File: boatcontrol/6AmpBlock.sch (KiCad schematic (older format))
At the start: 13 parts, among them U7901 ULN2803A

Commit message: Switch resistors
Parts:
- removed C7901, C7902, C7903, C7904, C7905, C7906, C7907, C7908: 107CKS016M 100UF, Capacitor_THT:CP_Radial_D5.0mm_P2.00mm, symbol Device:C_Small
- removed RN7901, RN7904: 4116R-1-103LF, DIP787W49P254L2197H469Q16N, symbol BoatControl:4116R-1-103LF
- removed RN7903: 4120R-1-103LF, BoatControl:DIP254P762X432-16P, symbol Device:R_Pack08
- added C5201, C5202, C5203, C5204, C5205, C5206, C5207, C5208: 1uF, Capacitor_THT:C_Disc_D7.5mm_W5.0mm_P5.00mm, symbol Device:C_Small
- added RN?: 10M Ohm, Resistor_THT:R_Array_SIP9, symbol Device:R_Network08
- added RN? (x2): 100K Ohm, Resistor_THT:R_Array_SIP9, symbol Device:R_Network08
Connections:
- wire segments 226 -> 205

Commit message: Resistance is futile
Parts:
- gave numbers to parts that had none: 3
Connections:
- net +5V: now also RN7904.1 (common)
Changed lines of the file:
@@
 $Descr A4 11693 8268
 encoding utf-8
-Sheet 79 87
+Sheet 52 87
 Title "Boat Control Hat"
 Date "2020-07-09"
@@
 AR Path="/D1BB8DB4/5F317CB5/60365AE4" Ref="#PWR07901"  Part="1"
 AR Path="/D1BB8DB4/5F746103/60365AE4" Ref="#PWR05201"  Part="1"
-F 0 "#PWR07901" H 6700 3400 50  0001 C CNN
+F 0 "#PWR05201" H 6700 3400 50  0001 C CNN
 F 1 "+12P" H 6550 3650 50  0000 C CNN
 F 2 "" H 6700 3550 50  0001 C CNN
@@
 AR Path="/D1BB8DB4/5F317CB5/60365AF1" Ref="U7901"  Part="1"
 AR Path="/D1BB8DB4/5F746103/60365AF1" Ref="U5201"  Part="1"
-F 0 "U7901" H 6250 3650 50  0000 L CNN
+F 0 "U5201" H 6250 3650 50  0000 L CNN
 F 1 "ULN2803A" H 6100 4350 50  0000 L CNN
 F 2 "Package_DIP:DIP-18_W7.62mm" H 6350 3200 50  0001 L CNN
@@
 AR Path="/D1BB8DB4/5F317CB5/60365B03" Ref="#PWR07902"  Part="1"
 AR Path="/D1BB8DB4/5F746103/60365B03" Ref="#PWR05202"  Part="1"
-F 0 "#PWR07902" H 6300 4300 50  0001 C CNN
+F 0 "#PWR05202" H 6300 4300 50  0001 C CNN
 F 1 "GND" H 6305 4377 50  0000 C CNN
 F 2 "" H 6300 4550 50  0001 C CNN
@@
 AR Path="/D1BB8DB4/5F317CB5/60365B8C" Ref="#PWR07903"  Part="1"
 AR Path="/D1BB8DB4/5F746103/60365B8C" Ref="#PWR05203"  Part="1"
-F 0 "#PWR07903" H 2250 5150 50  0001 C CNN
+F 0 "#PWR05203" H 2250 5150 50  0001 C CNN
 F 1 "+5V" H 2265 5473 50  0000 C CNN
 F 2 "" H 2250 5300 50  0001 C CNN
@@
 AR Path="/D1BB8DB4/5F317CB5/60365C68" Ref="RN7902"  Part="1"
 AR Path="/D1BB8DB4/5F746103/60365C68" Ref="RN5202"  Part="1"
-F 0 "RN7902" V 7000 4050 50  0000 L CNN
+F 0 "RN5202" V 7000 4050 50  0000 L CNN
 F 1 "4116R-1-471" V 7000 3900 50  0001 L CNN
 F 2 "BoatControl:DIP254P762X432-16P" V 7975 4050 50  0001 C CNN
@@
 AR Path="/D1BB8DB4/5F746103/62AB509B" Ref="C5201"  Part="1"
 AR Path="/D1BB8DB4/5F317CB5/62AB509B" Ref="C7901"  Part="1"
-F 0 "C7901" V 4400 2700 50  0000 L CNN
+F 0 "C5201" V 4400 2700 50  0000 L CNN
 F 1 "1uF" H 3600 2550 50  0001 L CNN
 F 2 "Capacitor_THT:C_Disc_D7.5mm_W5.0mm_P5.00mm" H 4450 2650 50  0001 C CNN
@@
 AR Path="/D1BB8DB4/5F746103/62AC1E93" Ref="C5202"  Part="1"
 AR Path="/D1BB8DB4/5F317CB5/62AC1E93" Ref="C7902"  Part="1"
-F 0 "C7902" V 4400 2900 50  0000 L CNN
+F 0 "C5202" V 4400 2900 50  0000 L CNN
 F 1 "1uF" H 3600 2750 50  0001 L CNN
 F 2 "Capacitor_THT:C_Disc_D7.5mm_W5.0mm_P5.00mm" H 4450 2850 50  0001 C CNN
@@
 AR Path="/D1BB8DB4/5F746103/62ADD9A6" Ref="C5208"  Part="1"
 AR Path="/D1BB8DB4/5F317CB5/62ADD9A6" Ref="C7908"  Part="1"
-F 0 "C7908" V 4400 5900 50  0000 L CNN
+F 0 "C5208" V 4400 5900 50  0000 L CNN
 F 1 "1uF" H 3600 5750 50  0001 L CNN
 F 2 "Capacitor_THT:C_Disc_D7.5mm_W5.0mm_P5.00mm" H 4450 5850 50  0001 C CNN
@@
 AR Path="/D1BB8DB4/5F746103/62AEACF8" Ref="C5207"  Part="1"
 AR Path="/D1BB8DB4/5F317CB5/62AEACF8" Ref="C7907"  Part="1"
-F 0 "C7907" V 4400 5700 50  0000 L CNN
+F 0 "C5207" V 4400 5700 50  0000 L CNN
 F 1 "1uF" H 3600 5550 50  0001 L CNN
 F 2 "Capacitor_THT:C_Disc_D7.5mm_W5.0mm_P5.00mm" H 4450 5650 50  0001 C CNN
@@
 AR Path="/D1BB8DB4/5F746103/62AF81A3" Ref="C5206"  Part="1"
 AR Path="/D1BB8DB4/5F317CB5/62AF81A3" Ref="C7906"  Part="1"
-F 0 "C7906" V 4400 4900 50  0000 L CNN
+F 0 "C5206" V 4400 4900 50  0000 L CNN
 F 1 "1uF" H 3600 4750 50  0001 L CNN
 F 2 "Capacitor_THT:C_Disc_D7.5mm_W5.0mm_P5.00mm" H 4450 4850 50  0001 C CNN
@@
 AR Path="/D1BB8DB4/5F746103/62B05762" Ref="C5205"  Part="1"
 AR Path="/D1BB8DB4/5F317CB5/62B05762" Ref="C7905"  Part="1"
-F 0 "C7905" V 4400 4700 50  0000 L CNN
+F 0 "C5205" V 4400 4700 50  0000 L CNN
 F 1 "1uF" H 3600 4550 50  0001 L CNN
 F 2 "Capacitor_THT:C_Disc_D7.5mm_W5.0mm_P5.00mm" H 4450 4650 50  0001 C CNN
@@
 AR Path="/D1BB8DB4/5F746103/62B3C5BA" Ref="C5203"  Part="1"
 AR Path="/D1BB8DB4/5F317CB5/62B3C5BA" Ref="C7903"  Part="1"
-F 0 "C7903" V 4400 3700 50  0000 L CNN
+F 0 "C5203" V 4400 3700 50  0000 L CNN
 F 1 "1uF" H 3600 3550 50  0001 L CNN
 F 2 "Capacitor_THT:C_Disc_D7.5mm_W5.0mm_P5.00mm" H 4450 3650 50  0001 C CNN
@@
 AR Path="/D1BB8DB4/5F746103/62B4996D" Ref="C5204"  Part="1"
 AR Path="/D1BB8DB4/5F317CB5/62B4996D" Ref="C7904"  Part="1"
-F 0 "C7904" V 4400 3900 50  0000 L CNN
+F 0 "C5204" V 4400 3900 50  0000 L CNN
 F 1 "1uF" H 3600 3750 50  0001 L CNN
 F 2 "Capacitor_THT:C_Disc_D7.5mm_W5.0mm_P5.00mm" H 4450 3850 50  0001 C CNN
@@
 AR Path="/D16552B4/5FA17F52/62C7A7CE" Ref="RN?"  Part="1"
 AR Path="/D16552B4/5FA17F6C/62C7A7CE" Ref="RN?"  Part="1"
-AR Path="/D1BB8DB4/5F317CB5/62C7A7CE" Ref="RN?"  Part="1"
-AR Path="/D1BB8DB4/5F746103/62C7A7CE" Ref="RN?"  Part="1"
-F 0 "RN?" V 1950 4050 50  0000 L CNN
+AR Path="/D1BB8DB4/5F317CB5/62C7A7CE" Ref="RN7903"  Part="1"
+AR Path="/D1BB8DB4/5F746103/62C7A7CE" Ref="RN5203"  Part="1"
+F 0 "RN5203" V 1950 4050 50  0000 L CNN
 F 1 "10M Ohm" H 2100 3700 50  0001 L CNN
 F 2 "Resistor_THT:R_Array_SIP9" V 2925 4100 50  0001 C CNN
@@
 Connection ~ 2250 3700
 Wire Wire Line
-	2250 3700 2250 5300
+	2250 3700 2250 4600
 $Comp
 L Device:R_Network08 RN?
@@
 AR Path="/D16552B4/5FA17F6C/62F1D24C" Ref="RN?"  Part="1"
 AR Path="/D16552B4/5FA17F86/62F1D24C" Ref="RN?"  Part="1"
-F 0 "RN?" V 1950 5000 50  0000 C CNN
+AR Path="/D1BB8DB4/5F317CB5/62F1D24C" Ref="RN7904"  Part="1"
+AR Path="/D1BB8DB4/5F746103/62F1D24C" Ref="RN5204"  Part="1"
+F 0 "RN5204" V 1950 5000 50  0000 C CNN
 F 1 "100K Ohm" V 2250 4700 50  0001 C CNN
 F 2 "Resistor_THT:R_Array_SIP9" H 3200 5100 50  0001 L CNN
@@
 AR Path="/D16552B4/5FA17F6C/62F2A731" Ref="RN?"  Part="1"
 AR Path="/D16552B4/5FA17F86/62F2A731" Ref="RN?"  Part="1"
-F 0 "RN?" V 1950 3200 50  0000 C CNN
+AR Path="/D1BB8DB4/5F317CB5/62F2A731" Ref="RN7901"  Part="1"
+AR Path="/D1BB8DB4/5F746103/62F2A731" Ref="RN5201"  Part="1"
+F 0 "RN5201" V 1950 3200 50  0000 C CNN
 F 1 "100K Ohm" V 2250 2900 50  0001 C CNN
 F 2 "Resistor_THT:R_Array_SIP9" H 3200 3300 50  0001 L CNN
@@
 Wire Wire Line
 	2650 5300 3200 5300
+Wire Wire Line
+	2250 4600 2250 3700
+Connection ~ 2250 4600
+Wire Wire Line
+	2250 4600 2250 5300
 $EndSCHEMATC

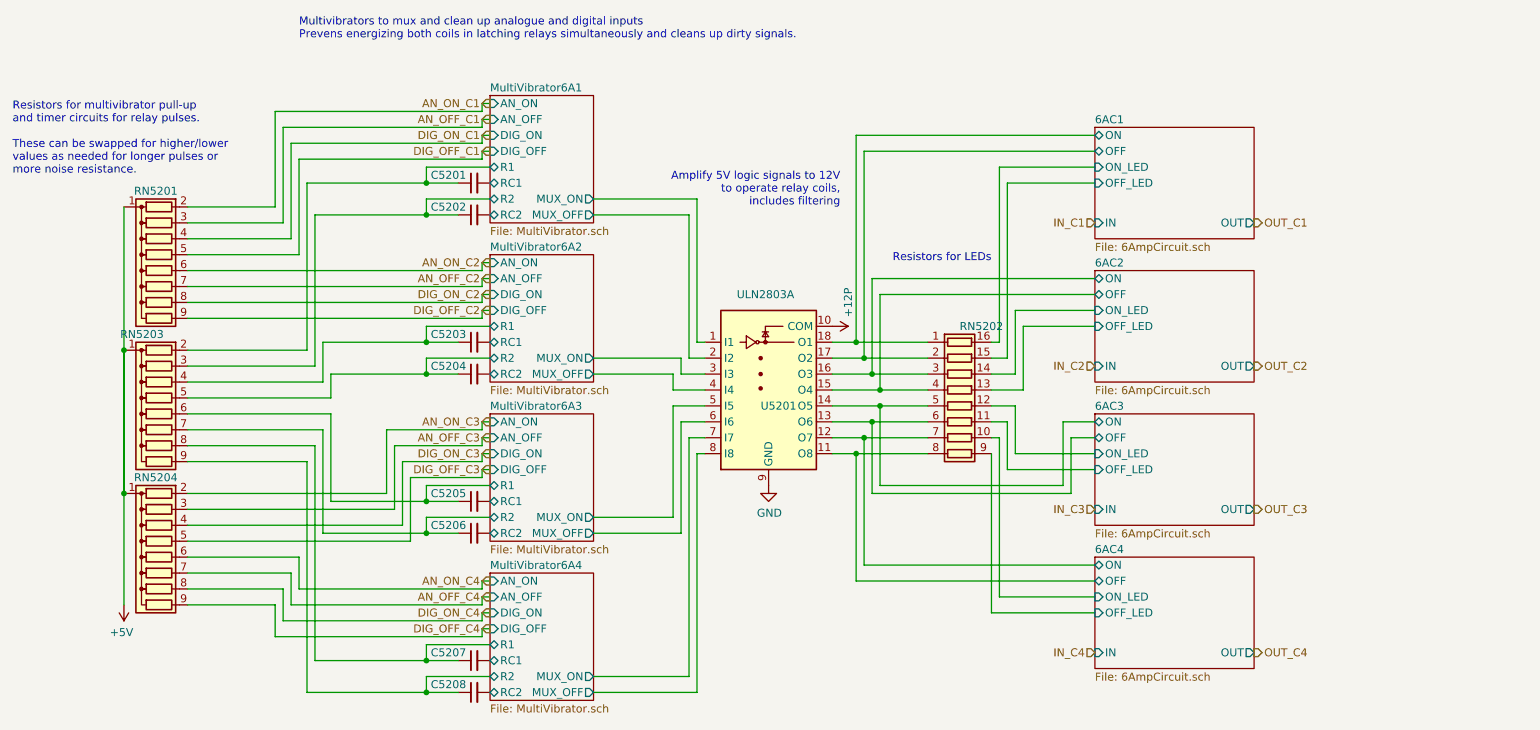
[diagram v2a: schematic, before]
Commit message: Remove resistor on protection, change MOSFET
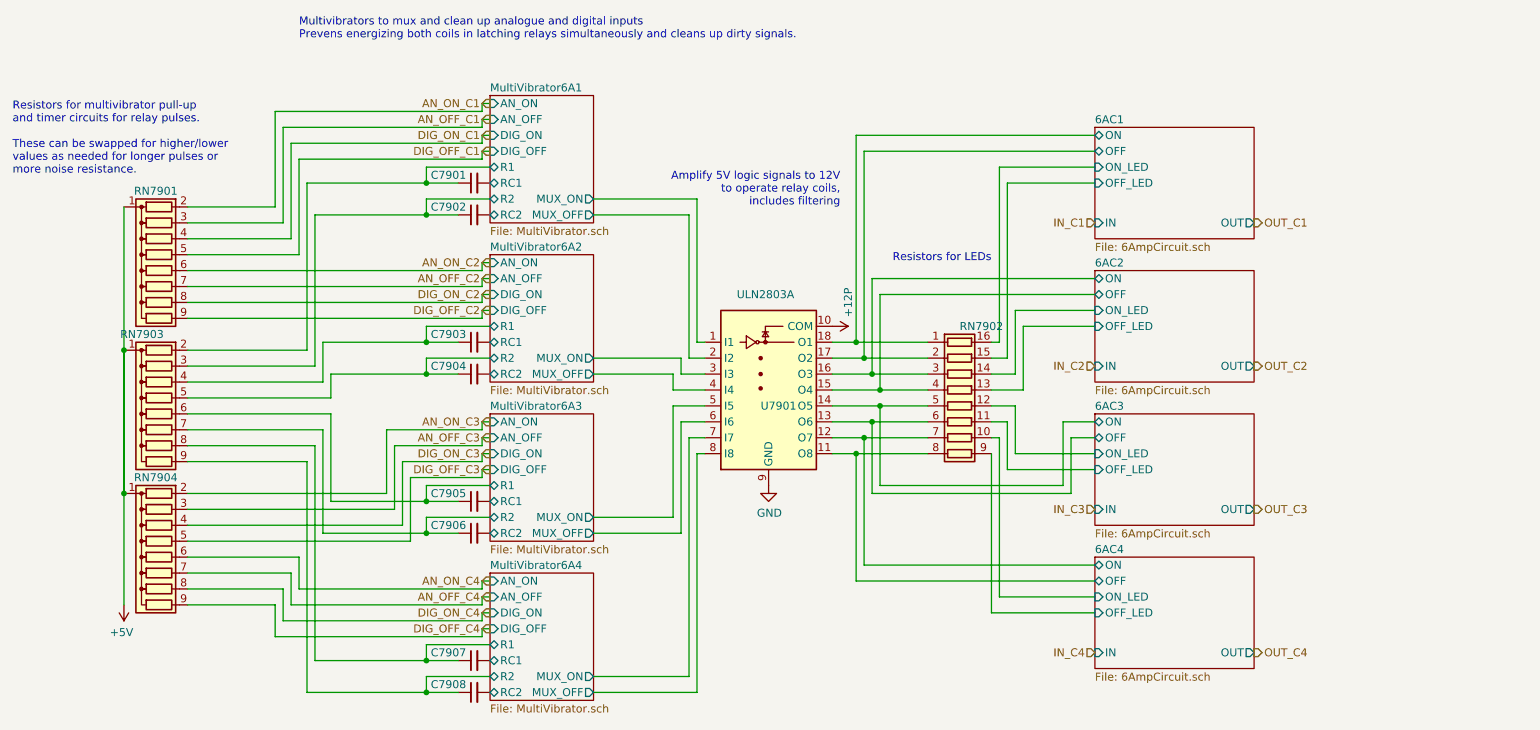
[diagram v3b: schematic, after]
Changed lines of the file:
@@
 $Descr A4 11693 8268
 encoding utf-8
-Sheet 52 87
+Sheet 79 87
 Title "Boat Control Hat"
 Date "2020-07-09"
@@
 AR Path="/D1BB8DB4/5F317CB5/60365AE4" Ref="#PWR07901"  Part="1"
 AR Path="/D1BB8DB4/5F746103/60365AE4" Ref="#PWR05201"  Part="1"
-F 0 "#PWR05201" H 6700 3400 50  0001 C CNN
+F 0 "#PWR07901" H 6700 3400 50  0001 C CNN
 F 1 "+12P" H 6550 3650 50  0000 C CNN
 F 2 "" H 6700 3550 50  0001 C CNN
@@
 AR Path="/D1BB8DB4/5F317CB5/60365AF1" Ref="U7901"  Part="1"
 AR Path="/D1BB8DB4/5F746103/60365AF1" Ref="U5201"  Part="1"
-F 0 "U5201" H 6250 3650 50  0000 L CNN
+F 0 "U7901" H 6250 3650 50  0000 L CNN
 F 1 "ULN2803A" H 6100 4350 50  0000 L CNN
 F 2 "Package_DIP:DIP-18_W7.62mm" H 6350 3200 50  0001 L CNN
@@
 AR Path="/D1BB8DB4/5F317CB5/60365B03" Ref="#PWR07902"  Part="1"
 AR Path="/D1BB8DB4/5F746103/60365B03" Ref="#PWR05202"  Part="1"
-F 0 "#PWR05202" H 6300 4300 50  0001 C CNN
+F 0 "#PWR07902" H 6300 4300 50  0001 C CNN
 F 1 "GND" H 6305 4377 50  0000 C CNN
 F 2 "" H 6300 4550 50  0001 C CNN
@@
 AR Path="/D1BB8DB4/5F317CB5/60365B8C" Ref="#PWR07903"  Part="1"
 AR Path="/D1BB8DB4/5F746103/60365B8C" Ref="#PWR05203"  Part="1"
-F 0 "#PWR05203" H 2250 5150 50  0001 C CNN
+F 0 "#PWR07903" H 2250 5150 50  0001 C CNN
 F 1 "+5V" H 2265 5473 50  0000 C CNN
 F 2 "" H 2250 5300 50  0001 C CNN
@@
 AR Path="/D1BB8DB4/5F317CB5/60365C68" Ref="RN7902"  Part="1"
 AR Path="/D1BB8DB4/5F746103/60365C68" Ref="RN5202"  Part="1"
-F 0 "RN5202" V 7000 4050 50  0000 L CNN
+F 0 "RN7902" V 7000 4050 50  0000 L CNN
 F 1 "4116R-1-471" V 7000 3900 50  0001 L CNN
 F 2 "BoatControl:DIP254P762X432-16P" V 7975 4050 50  0001 C CNN
@@
 AR Path="/D1BB8DB4/5F746103/62AB509B" Ref="C5201"  Part="1"
 AR Path="/D1BB8DB4/5F317CB5/62AB509B" Ref="C7901"  Part="1"
-F 0 "C5201" V 4400 2700 50  0000 L CNN
+F 0 "C7901" V 4400 2700 50  0000 L CNN
 F 1 "1uF" H 3600 2550 50  0001 L CNN
 F 2 "Capacitor_THT:C_Disc_D7.5mm_W5.0mm_P5.00mm" H 4450 2650 50  0001 C CNN
@@
 AR Path="/D1BB8DB4/5F746103/62AC1E93" Ref="C5202"  Part="1"
 AR Path="/D1BB8DB4/5F317CB5/62AC1E93" Ref="C7902"  Part="1"
-F 0 "C5202" V 4400 2900 50  0000 L CNN
+F 0 "C7902" V 4400 2900 50  0000 L CNN
 F 1 "1uF" H 3600 2750 50  0001 L CNN
 F 2 "Capacitor_THT:C_Disc_D7.5mm_W5.0mm_P5.00mm" H 4450 2850 50  0001 C CNN
@@
 AR Path="/D1BB8DB4/5F746103/62ADD9A6" Ref="C5208"  Part="1"
 AR Path="/D1BB8DB4/5F317CB5/62ADD9A6" Ref="C7908"  Part="1"
-F 0 "C5208" V 4400 5900 50  0000 L CNN
+F 0 "C7908" V 4400 5900 50  0000 L CNN
 F 1 "1uF" H 3600 5750 50  0001 L CNN
 F 2 "Capacitor_THT:C_Disc_D7.5mm_W5.0mm_P5.00mm" H 4450 5850 50  0001 C CNN
@@
 AR Path="/D1BB8DB4/5F746103/62AEACF8" Ref="C5207"  Part="1"
 AR Path="/D1BB8DB4/5F317CB5/62AEACF8" Ref="C7907"  Part="1"
-F 0 "C5207" V 4400 5700 50  0000 L CNN
+F 0 "C7907" V 4400 5700 50  0000 L CNN
 F 1 "1uF" H 3600 5550 50  0001 L CNN
 F 2 "Capacitor_THT:C_Disc_D7.5mm_W5.0mm_P5.00mm" H 4450 5650 50  0001 C CNN
@@
 AR Path="/D1BB8DB4/5F746103/62AF81A3" Ref="C5206"  Part="1"
 AR Path="/D1BB8DB4/5F317CB5/62AF81A3" Ref="C7906"  Part="1"
-F 0 "C5206" V 4400 4900 50  0000 L CNN
+F 0 "C7906" V 4400 4900 50  0000 L CNN
 F 1 "1uF" H 3600 4750 50  0001 L CNN
 F 2 "Capacitor_THT:C_Disc_D7.5mm_W5.0mm_P5.00mm" H 4450 4850 50  0001 C CNN
@@
 AR Path="/D1BB8DB4/5F746103/62B05762" Ref="C5205"  Part="1"
 AR Path="/D1BB8DB4/5F317CB5/62B05762" Ref="C7905"  Part="1"
-F 0 "C5205" V 4400 4700 50  0000 L CNN
+F 0 "C7905" V 4400 4700 50  0000 L CNN
 F 1 "1uF" H 3600 4550 50  0001 L CNN
 F 2 "Capacitor_THT:C_Disc_D7.5mm_W5.0mm_P5.00mm" H 4450 4650 50  0001 C CNN
@@
 AR Path="/D1BB8DB4/5F746103/62B3C5BA" Ref="C5203"  Part="1"
 AR Path="/D1BB8DB4/5F317CB5/62B3C5BA" Ref="C7903"  Part="1"
-F 0 "C5203" V 4400 3700 50  0000 L CNN
+F 0 "C7903" V 4400 3700 50  0000 L CNN
 F 1 "1uF" H 3600 3550 50  0001 L CNN
 F 2 "Capacitor_THT:C_Disc_D7.5mm_W5.0mm_P5.00mm" H 4450 3650 50  0001 C CNN
@@
 AR Path="/D1BB8DB4/5F746103/62B4996D" Ref="C5204"  Part="1"
 AR Path="/D1BB8DB4/5F317CB5/62B4996D" Ref="C7904"  Part="1"
-F 0 "C5204" V 4400 3900 50  0000 L CNN
+F 0 "C7904" V 4400 3900 50  0000 L CNN
 F 1 "1uF" H 3600 3750 50  0001 L CNN
 F 2 "Capacitor_THT:C_Disc_D7.5mm_W5.0mm_P5.00mm" H 4450 3850 50  0001 C CNN
@@
 AR Path="/D1BB8DB4/5F317CB5/62C7A7CE" Ref="RN7903"  Part="1"
 AR Path="/D1BB8DB4/5F746103/62C7A7CE" Ref="RN5203"  Part="1"
-F 0 "RN5203" V 1950 4050 50  0000 L CNN
+F 0 "RN7903" V 1950 4050 50  0000 L CNN
 F 1 "10M Ohm" H 2100 3700 50  0001 L CNN
 F 2 "Resistor_THT:R_Array_SIP9" V 2925 4100 50  0001 C CNN
@@
 AR Path="/D1BB8DB4/5F317CB5/62F1D24C" Ref="RN7904"  Part="1"
 AR Path="/D1BB8DB4/5F746103/62F1D24C" Ref="RN5204"  Part="1"
-F 0 "RN5204" V 1950 5000 50  0000 C CNN
+F 0 "RN7904" V 1950 5000 50  0000 C CNN
 F 1 "100K Ohm" V 2250 4700 50  0001 C CNN
 F 2 "Resistor_THT:R_Array_SIP9" H 3200 5100 50  0001 L CNN
@@
 AR Path="/D1BB8DB4/5F317CB5/62F2A731" Ref="RN7901"  Part="1"
 AR Path="/D1BB8DB4/5F746103/62F2A731" Ref="RN5201"  Part="1"
-F 0 "RN5201" V 1950 3200 50  0000 C CNN
+F 0 "RN7901" V 1950 3200 50  0000 C CNN
 F 1 "100K Ohm" V 2250 2900 50  0001 C CNN
 F 2 "Resistor_THT:R_Array_SIP9" H 3200 3300 50  0001 L CNN

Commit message: Fix graphics
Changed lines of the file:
@@
 $Descr A4 11693 8268
 encoding utf-8
-Sheet 79 87
+Sheet 52 87
 Title "Boat Control Hat"
 Date "2020-07-09"
@@
 Wire Wire Line
 	2650 5300 3200 5300
-Wire Wire Line
-	2250 4600 2250 3700
 Connection ~ 2250 4600
 Wire Wire Line
